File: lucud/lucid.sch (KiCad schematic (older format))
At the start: 0 parts

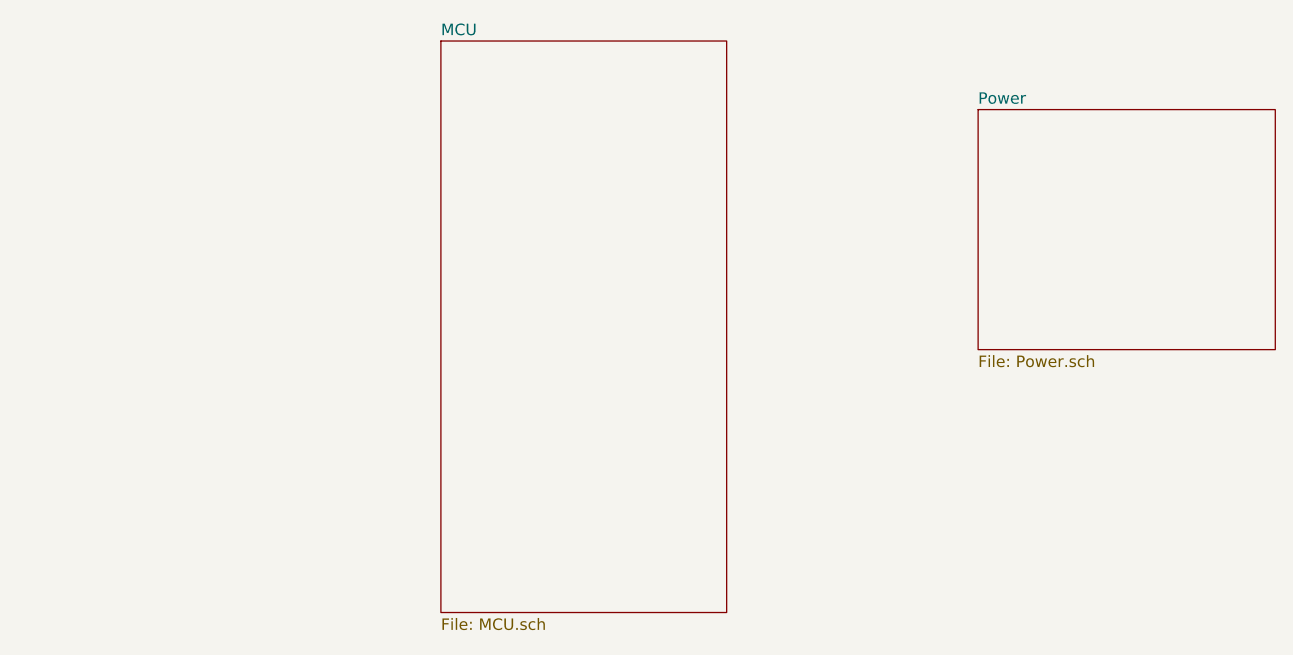
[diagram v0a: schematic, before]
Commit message: Added power headers and some caps for the pcb.
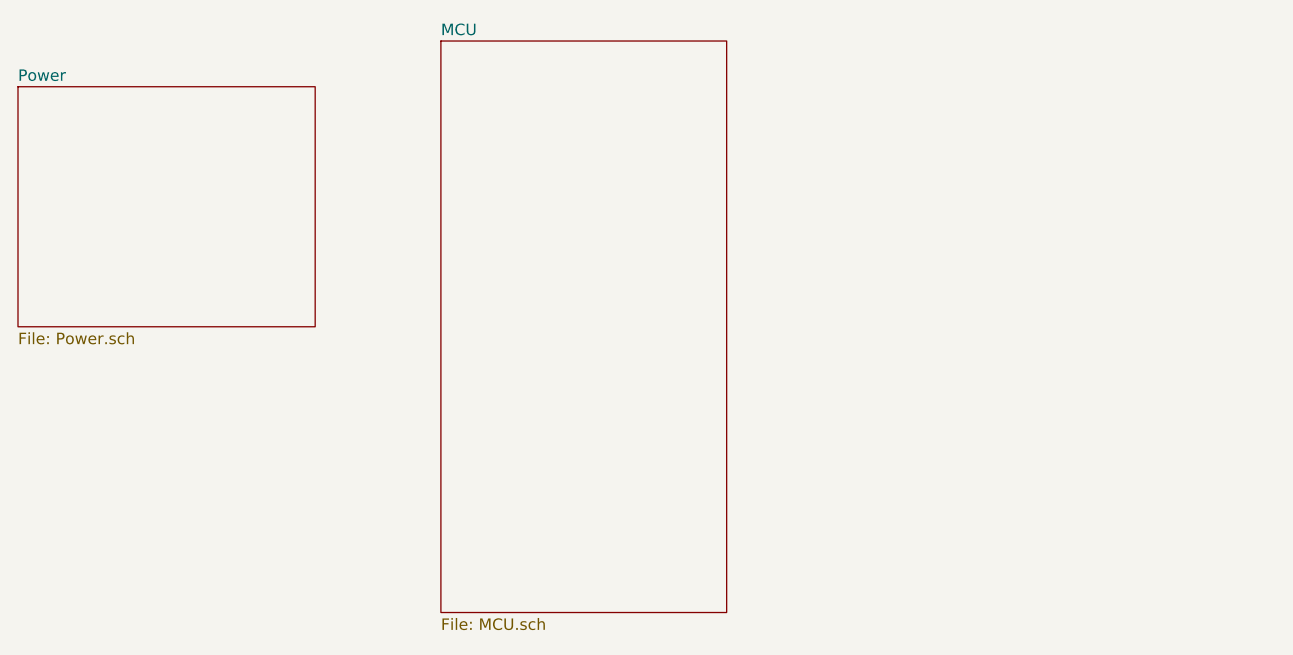
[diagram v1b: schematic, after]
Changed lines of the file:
@@
 $EndSheet
 $Sheet
-S 5400 1600 1300 1050
+S 1200 1500 1300 1050
 U 5C243B4D
 F0 "Power" 50
